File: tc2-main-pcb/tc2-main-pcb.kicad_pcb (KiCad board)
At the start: 4 copper layers, 73 x 75.5 mm, 191 parts, among them J1 Screw_Terminal_01x01, J10 Conn_02x06_Odd_Even, J11 Conn_01x08, J12 USB_B_Micro, J2 Screw_Terminal_01x01, J3 Conn_01x03, J4 Raspberry_Pi_2_3, J5 Screw_Terminal_01x01, J6 Screw_Terminal_01x01, J7 Screw_Terminal_01x01, J8 Screw_Terminal_01x01, J9 Conn_02x03_Odd_Even, Q1 Q_PMOS_GSD, SW1 SW_Push, U1 ATtiny1616-M, U10 TD6810, U11 TD6810, U12 SIM7600G-H-M.2, U13 AHT20_C2757850, U14 MAX98357AEWL+T, U15 74HC4052, U16 M24C02-WMN, U18 TCA4311ADGKR, U2 W25Q128JVS, U3 RP2040, U4 MT29F2G01ABAGDWB-IT, U5 TPS6302x, U6 PCF8563T, U7 ME6216A28XG, U8 Flir_LEPTON, U9 3N25000G33YC, Y1 Crystal_GND24, Y2 Crystal

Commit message: panelize WIP
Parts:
- added REF**: Tab, kikit:Tab, F.Cu at (12.2, -28.0)
- added REF**: Tab, kikit:Tab, F.Cu at (-54.8, -22.0)
- added REF**: Tab, kikit:Tab, F.Cu at (3.80, -37.0)
- added REF**: Tab, kikit:Tab, F.Cu at (-61.8, 20.0)
- added REF**: Tab, kikit:Tab, F.Cu at (-5.79, 34.0)
- added REF**: Tab, kikit:Tab, F.Cu at (-36.2, -37.0)
- added REF**: Tab, kikit:Tab, F.Cu at (12.8, 22.0)
- added REF**: Tab, kikit:Tab, F.Cu at (-16.2, -37.0)
- added REF**: Tab, kikit:Tab, F.Cu at (-51.8, 27.0)
- BT1, C1, C16, C17, C18, C19, C2, C20, C21, C22, C23, C24, C32, C33, C34, C35, C36, C39, C40, C51, C56, C57, C58, C59, C61, C62, C63, D2, D3, J1, J10, J11, J12, J2, J3, J4, J5, J6, J8, R1, R10, R11, R13, R14, R15, R17, R2, R25, R26, R27, R32, R35, R36, R37, R39, R46, R49, R50, R51, R6, R7, R8, TP17, U1, U12, U13, U2, U4, U6, U7, U9, Y2: moved to F.Cu
- C10, C11, C12, C13, C14, C15, C25, C26, C27, C28, C29, C3, C30, C31, C37, C38, C4, C41, C42, C43, C44, C45, C46, C47, C48, C49, C5, C50, C52, C53, C54, C55, C6, C60, C64, C65, C66, C7, C8, C9, FB1, H1, H2, H3, H4, H5, H6, J7, J9, L1, L2, L3, LED1, Q1, R12, R16, R18, R19, R20, R21, R22, R23, R24, R28, R29, R3, R30, R31, R33, R34, R38, R4, R40, R41, R42, R43, R44, R45, R47, R48, R5, R52, R53, R9, SW1, TP1, TP10, TP11, TP12, TP13, TP14, TP15, TP16, TP18, TP19, TP2, TP20, TP21, TP22, TP26, TP27, TP3, TP4, TP40, TP41, TP5, TP6, TP7, TP8, U10, U11, U14, U15, U16, U18, U3, U5, U8, Y1: moved to B.Cu
- moved H2 113.6 mm to (-56.8, 18.0), turned to 180 degrees
- moved J11 103.4 mm to (-51.7, -11.0), turned to 0 degrees
- moved J1 98.0 mm to (-49.0, -29.0), turned to 0 degrees
- moved J8 98.0 mm to (-49.0, 21.0), turned to 0 degrees
- moved C33 89.8 mm to (-44.9, 10.2)
- moved C36 87.4 mm to (-43.7, 10.8)
- moved TP18 86.7 mm to (-43.3, -16.5), turned to 180 degrees
- moved TP14 86.6 mm to (-43.3, -18.3), turned to 180 degrees
- moved C34 85.0 mm to (-42.5, 10.2)
- moved C25 84.4 mm to (-42.2, 3.58)
- moved TP19 84.2 mm to (-42.1, -1.90), turned to 180 degrees
- moved H1 83.6 mm to (-41.8, -29.0), turned to 180 degrees
- moved FB1 83.6 mm to (-41.8, 15.3)
- moved C40 82.7 mm to (-41.3, 10.8)
- moved TP20 82.4 mm to (-41.2, -8.00), turned to 180 degrees
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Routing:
- added copper zone on B.Cu, net +3V3_rp2040
- added copper zone on B.Cu, net /Lepton/SW_1V2
- added copper zone on B.Cu, net /Lepton/SW_3V0
- added copper zone on B.Cu, net /modem/3V3_L1
- added copper zone on B.Cu, net /modem/3V3_L2
- added copper zone on B.Cu, net /modem/MODEM_3V8
- removed copper zone on F.Cu, net +3V3_rp2040
- removed copper zone on F.Cu, net /Lepton/SW_1V2
- removed copper zone on F.Cu, net /Lepton/SW_3V0
- removed copper zone on F.Cu, net /modem/3V3_L1
- removed copper zone on F.Cu, net /modem/3V3_L2
- removed copper zone on F.Cu, net /modem/MODEM_3V8
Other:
- outline, holes or cut-outs redrawn

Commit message: Adding panel
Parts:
- removed the REF** at (12.2, -28.0)
- removed the REF** at (-54.8, -22.0)
- removed the REF** at (3.80, -37.0)
- removed the REF** at (-61.8, 20.0)
- removed the REF** at (-5.79, 34.0)
- removed the REF** at (-36.2, -37.0)
- removed the REF** at (12.8, 22.0)
- removed the REF** at (-16.2, -37.0)
- removed the REF** at (-51.8, 27.0)
- added REF**: Tab_8mm, kikit:Tab_8mm, F.Cu at (12.2, 22.0)
- added REF**: Tab_8mm, kikit:Tab_8mm, F.Cu at (-36.2, -36.4)
- added REF**: Tab_8mm, kikit:Tab_8mm, F.Cu at (3.80, -36.3)
- added REF**: Tab_8mm, kikit:Tab_8mm, F.Cu at (12.6, -28.0)
- added REF**: Tab_8mm, kikit:Tab_8mm, F.Cu at (-62.1, 20.0)
- added REF**: Tab_8mm, kikit:Tab_8mm, F.Cu at (-5.80, 34.3)
- added REF**: Tab_8mm, kikit:Tab_8mm, F.Cu at (-55.1, -22.0)
- added REF**: Tab_8mm, kikit:Tab_8mm, F.Cu at (-51.8, 27.3)
- added REF**: Tab_8mm, kikit:Tab_8mm, F.Cu at (-16.2, -36.4)

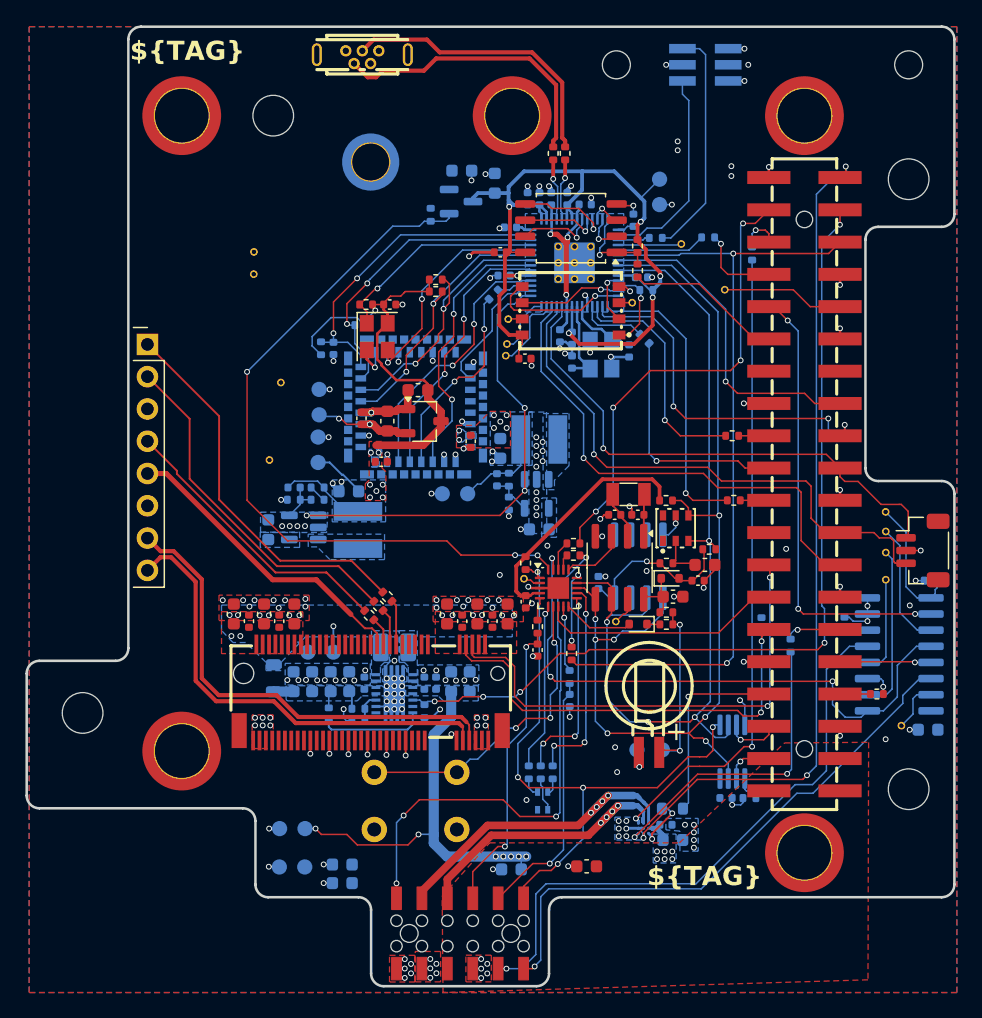
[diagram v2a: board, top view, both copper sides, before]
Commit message: Update to use touch sensor
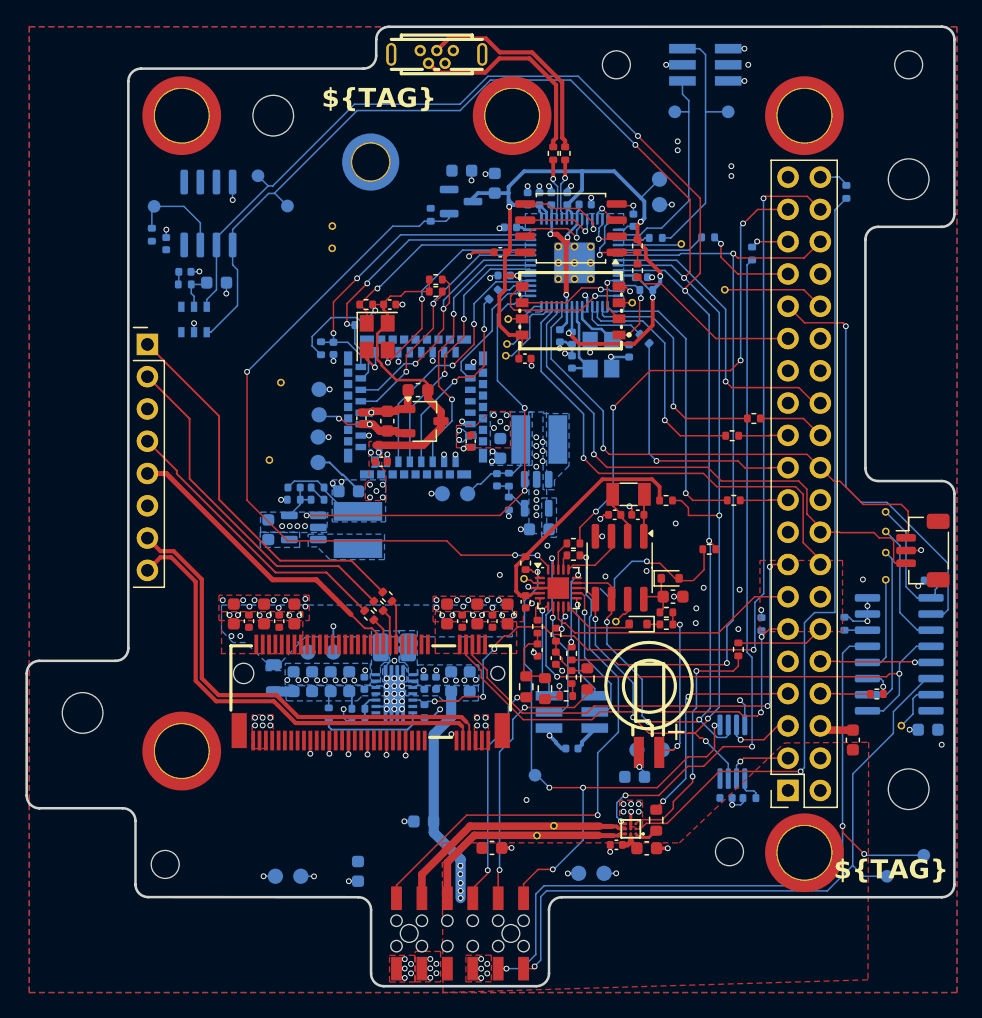
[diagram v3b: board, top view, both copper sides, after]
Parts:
- removed LED1: NH-B1515RGBA-HF, cacophony-library:LED-ARRAY-SMD_4P-L1.6-W1.5-TL_NH-B1515RGBA
- removed R3, R4, R5: 180R, Resistor_SMD:R_0402_1005Metric
- removed the REF** at (12.2, 22.0)
- removed the REF** at (-36.2, -36.4)
- removed the REF** at (3.80, -36.3)
- removed the REF** at (12.6, -28.0)
- removed the REF** at (-62.1, 20.0)
- removed the REF** at (-5.80, 34.3)
- removed the REF** at (-55.1, -22.0)
- removed the REF** at (-51.8, 27.3)
- removed the REF** at (-16.2, -36.4)
- removed SW1: SW_Push, Button_Switch_THT:SW_PUSH_6mm
- added C131: 22uF, Capacitor_SMD:C_0603_1608Metric, F.Cu at (3.81, 20.1)
- added C168: 220nF, Capacitor_SMD:C_0402_1005Metric, B.Cu at (-18.3, 20.8)
- added H107: MountingHole, cacophony-library:MountingHole_2.2mm_M2, F.Cu at (-50.3, 29.9)
- added H108: MountingHole, cacophony-library:MountingHole_2.2mm_M2, F.Cu at (-5.90, 28.9)
- added J113: Conn_02x03_Odd_Even, cacophony-library:mic-pcb, B.Cu at (-18.3, 17.9)
- added R115: 100k, Resistor_SMD:R_0402_1005Metric, B.Cu at (-51.4, -19.6)
- added R146: 1M, Resistor_SMD:R_0603_1608Metric, F.Cu at (-21.9, 15.9)
- added R148: 680k, Resistor_SMD:R_0603_1608Metric, F.Cu at (-20.4, 16.1)
- added R150: 1M, Resistor_SMD:R_0603_1608Metric, F.Cu at (-17.1, 15.3)
- added R152: 100k, Resistor_SMD:R_0402_1005Metric, F.Cu at (-18.3, 15.2)
- added R153: 68k, Resistor_SMD:R_0402_1005Metric, F.Cu at (-18.8, 16.7)
- added REF**: Tab8mm, cacophony-library:Tab8mm, F.Cu at (-55.1, -22.0)
- added REF**: Tab8mm, cacophony-library:Tab8mm, F.Cu at (-43.8, 35.3)
- added REF**: Tab8mm, cacophony-library:Tab8mm, F.Cu at (-5.80, 34.3)
- added REF**: Tab8mm, cacophony-library:Tab8mm, F.Cu at (-62.1, 20.0)
- added REF**: Tab8mm, cacophony-library:Tab8mm, F.Cu at (3.80, -36.3)
- added REF**: Tab8mm, cacophony-library:Tab8mm, F.Cu at (12.6, -28.0)
- added REF**: Tab8mm, cacophony-library:Tab8mm, F.Cu at (-16.2, -36.4)
- added REF**: Tab8mm, cacophony-library:Tab8mm, F.Cu at (-41.2, -36.4)
- added REF**: Tab8mm, cacophony-library:Tab8mm, F.Cu at (12.2, 22.0)
- added TP101: TestPoint, TestPoint:TestPoint_Pad_D1.0mm, B.Cu at (-6.00, -29.3)
- added TP102: TestPoint, TestPoint:TestPoint_Pad_D1.0mm, B.Cu at (-10.2, -29.3)
- added TP108: TestPoint, TestPoint:TestPoint_Pad_D1.0mm, B.Cu at (-40.7, -21.9)
- added TP110: TestPoint, TestPoint:TestPoint_Pad_D1.0mm, B.Cu at (-43.0, -24.3)
- added TP117: TestPoint, TestPoint:TestPoint_Pad_D1.0mm, B.Cu at (-51.2, -21.9)
- added TP120: TestPoint, cacophony-library:TP, F.Cu at (-21.1, 27.6)
- added TP121: TestPoint, TestPoint:TestPoint_Pad_D1.0mm, B.Cu at (-21.2, 22.9)
- added TP122: TestPoint, cacophony-library:TP, F.Cu at (-19.7, 26.9)
- added TP126: TestPoint, TestPoint:TestPoint_Pad_D1.0mm, B.Cu at (6.50, 30.9)
- added TP128: TestPoint, TestPoint:TestPoint_Pad_D1.0mm, B.Cu at (9.39, 29.2)
- C118: renamed from C17; moved to B.Cu
- C119: renamed from C39; moved to B.Cu
- C128: renamed from C28; moved to F.Cu
- C129: renamed from C29; moved to F.Cu
- C167: renamed from C44; moved to F.Cu
- J110: renamed from J4; footprint cacophony-library:HDR-SMD_40P-P2.54-V-F-R2-C20-LS8.2-EH -> cacophony-library:rpi-throughhole-socket
- R112: renamed from R39; moved to B.Cu
- R116: renamed from R12; moved to F.Cu
- R119: renamed from R34; moved to F.Cu
- R122: renamed from R31; moved to F.Cu
- R151: renamed from R40; moved to F.Cu
- U104: renamed from U13; moved to B.Cu
- U107: renamed from U14; moved to F.Cu
- moved C118 47.1 mm to (-48.8, -16.7)
- moved C119 44.4 mm to (-46.3, -15.9)
- moved R112 43.8 mm to (-48.8, -15.7)
- moved U106 43.8 mm to (-46.9, -21.3)
- moved C121 43.2 mm to (-50.2, -18.9)
- moved U104 41.3 mm to (-48.0, -13.0), turned to 90 degrees
- moved C124 24.5 mm to (-13.4, 23.0), turned to 0 degrees
- moved J110 24.1 mm to (-1.29, 24.1)
- moved TP119 23.8 mm to (-16.8, 30.6)
- moved C127 7.86 mm to (-30.0, 26.5)
- moved C126 7.59 mm to (-24.6, 28.6), turned to 0 degrees
- moved R122 6.78 mm to (-3.98, -5.17)
- moved TP104 6.50 mm to (-37.1, -20.3)
- moved TP105 6.50 mm to (-37.2, -18.6)
- moved J102 5.86 mm to (-28.9, -33.6)
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- renumbered BT1 to BT101, C5 to C101, C6 to C102, C8 to C103, C10 to C104, C11 to C105, C12 to C106, C13 to C107, C14 to C108, C15 to C109, C38 to C110, C43 to C111, C7 to C112, C9 to C113, C2 to C114, C3 to C115, C4 to C116, C16 to C117, C18 to C120, C48 to C121, C63 to C122, C61 to C123, C65 to C124, C66 to C125, C62 to C126, C64 to C127, C50 to C130, C37 to C132, C25 to C133, C41 to C134, C30 to C135, C26 to C136, C21 to C137, C23 to C138, C42 to C139, C31 to C140, C24 to C141, C19 to C142, C20 to C143, C22 to C144, C27 to C145, C54 to C146, C55 to C147, C47 to C148, C46 to C149, C45 to C150, C60 to C151, C49 to C152, C52 to C153, C53 to C154, C57 to C155, C58 to C156, C59 to C157, C51 to C158, C32 to C159, C33 to C160, C34 to C161, C35 to C162, C36 to C163, C40 to C164, C56 to C165, C1 to C166, D3 to D101, D2 to D102, FB1 to FB101, H5 to H101, H6 to H102, H1 to H103, H3 to H104, H4 to H105, H2 to H106, J9 to J101, J12 to J102, J3 to J103, J10 to J104, J2 to J105, J8 to J106, J1 to J107, J5 to J108, J6 to J109, J11 to J111, J7 to J112, L1 to L101, L2 to L102, L3 to L103, Q1 to Q101, R38 to R101, R50 to R102, R51 to R103, R28 to R104, R10 to R105, R53 to R106, R11 to R107, R2 to R108, R1 to R109, R48 to R110, R9 to R111, R7 to R113, R8 to R114, R52 to R117, R37 to R118, R29 to R120, R30 to R121, R14 to R123, R32 to R124, R41 to R125, R47 to R126, R33 to R127, R20 to R128, R21 to R129, R22 to R130, R23 to R131, R17 to R132, R18 to R133, R19 to R134, R16 to R135, R13 to R136, R36 to R137, R42 to R138, R43 to R139, R45 to R140, R44 to R141, R24 to R142, R25 to R143, R26 to R144, R27 to R145, R49 to R147, R6 to R149, R15 to R154, R46 to R155, R35 to R156, TP3 to TP103, TP14 to TP104, TP18 to TP105, TP19 to TP106, TP20 to TP107, TP12 to TP109, TP26 to TP111, TP27 to TP112, TP41 to TP113, TP40 to TP114, TP13 to TP115, TP17 to TP116, TP6 to TP118, TP10 to TP119, TP22 to TP123, TP16 to TP124, TP15 to TP125, TP21 to TP127, TP11 to TP129, TP7 to TP130, TP4 to TP131, TP8 to TP132, TP5 to TP133, TP1 to TP134, TP2 to TP135, U2 to U101, U3 to U102, U4 to U103, U6 to U105, U16 to U106, U18 to U108, U15 to U109, U10 to U110, U11 to U111, U7 to U112, U9 to U113, U8 to U114, U5 to U115, U12 to U116, U1 to U117, Y1 to Y101, Y2 to Y102
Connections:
- net BATT_SENSE_HIGH_VOLTAGE_PHY renamed BATT_SENSE_HV_PHY
- net BATT_SENSE_LOW_VOLTAGE_PHY renamed BATT_SENSE_LV_PHY
- C165 pad 2: BATT_SENSE_LV -> /ATtiny1616/BATT_SENSE_LV
- C167 pad 2: BATT_SENSE_HV -> /ATtiny1616/BATT_SENSE_HV
- J104 pad 3: BATT_SENSE_HV -> BATTERY_HV
- J104 pad 5: BATT_SENSE_LV -> BATTERY_LV
- J104 pad 7: SPEAKER_- -> SPEAKER_+
- J104 pad 9: SPEAKER_+ -> SPEAKER_-
- R147 pad 2: BATT_SENSE_LV -> /ATtiny1616/BATT_SENSE_LV
- R151 pad 2: BATT_SENSE_HV -> /ATtiny1616/BATT_SENSE_HV
- U106 pad 7: unconnected-(U16-~{WC}-Pad7) -> /EEPROM_~{WC}
- U117 pad 11: /ATtiny1616/~{LED_B_PHY} -> ~{LED_B}
- U117 pad 12: /ATtiny1616/~{LED_G_PHY} -> ~{LED_G}
- U117 pad 6: /ATtiny1616/~{LED_R_PHY} -> ~{LED_R}
- U117 pad 7: /ATtiny1616/ATtiny_SW -> ATtiny_SW
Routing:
- net SCL: track 71.8 -> 125.8 mm, vias 4 -> 6
- net SDA: track 79.9 -> 132.9 mm
- net /ATtiny1616/ATtiny_SW: track 24.7 -> 0.00 mm, vias 3 -> 0
- net BATT_SENSE_LV: track 23.7 -> 0.00 mm, vias 2 -> 0
- net BATTERY_HV: track 0.00 -> 21.6 mm, vias 0 -> 2
- net BATT_SENSE_HV: track 20.0 -> 0.00 mm, vias 1 -> 0
- net BATTERY_LV: track 0.00 -> 17.2 mm, vias 0 -> 2
- net /ATtiny1616/~{LED_G_PHY}: track 16.4 -> 0.00 mm, vias 3 -> 0
- net /ATtiny1616/~{LED_B_PHY}: track 15.6 -> 0.00 mm, vias 3 -> 0
- net +5V: track 34.4 -> 20.8 mm, vias 13 -> 6
- net /ATtiny1616/~{LED_R_PHY}: track 13.2 -> 0.00 mm, vias 1 -> 0
- net OUT_TX: track 47.0 -> 59.7 mm, vias 1 -> 3
- net GND: track 105.8 -> 96.1 mm, vias 183 -> 178
- net ~{LED_G}: track 1.32 -> 10.9 mm, vias 0 -> 1
- net ATtiny_SW: track 0.00 -> 9.01 mm, vias 0 -> 1
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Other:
- outline, holes or cut-outs redrawn

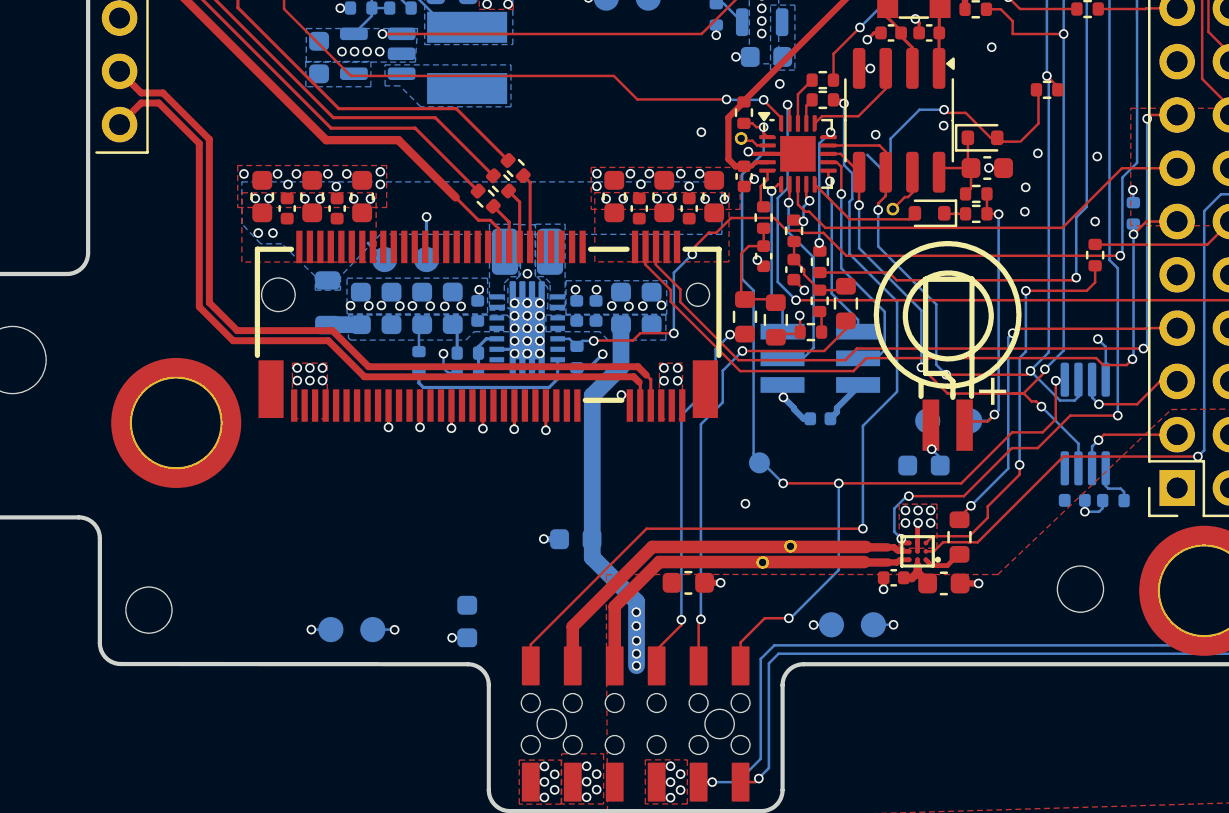
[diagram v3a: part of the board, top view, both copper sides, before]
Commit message: Change to through hole connector and add simcard PCB to pannel
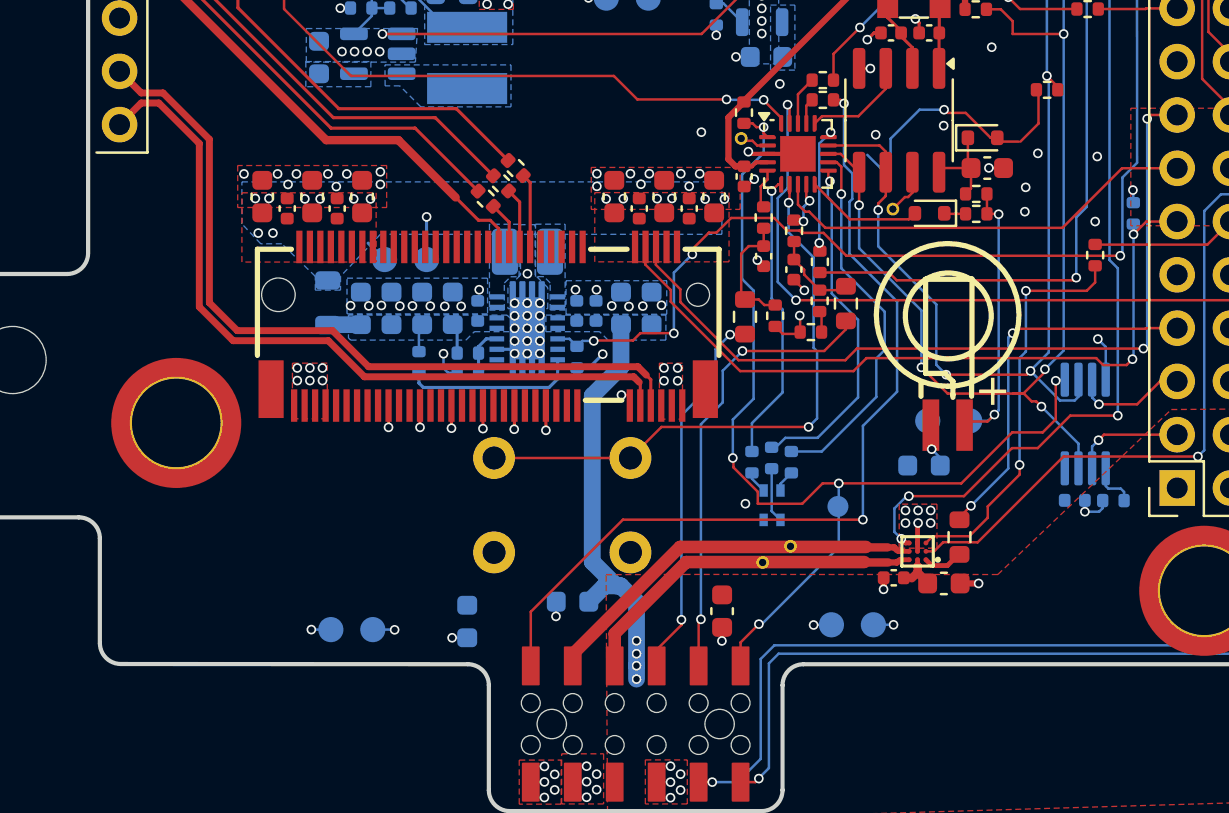
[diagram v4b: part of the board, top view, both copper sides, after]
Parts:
- removed C168: 220nF, Capacitor_SMD:C_0402_1005Metric
- removed H107, H108: MountingHole, cacophony-library:MountingHole_2.2mm_M2
- removed J113: Conn_02x03_Odd_Even, cacophony-library:mic-pcb
- removed R148: 680k, Resistor_SMD:R_0603_1608Metric
- added LED101: NH-B1515RGBA-HF, cacophony-library:LED-ARRAY-SMD_4P-L1.6-W1.5-TL_NH-B1515RGBA, B.Cu at (-20.6, 24.9)
- added R157: 180R, Resistor_SMD:R_0402_1005Metric, B.Cu at (-21.6, 22.9)
- added R158: 180R, Resistor_SMD:R_0402_1005Metric, B.Cu at (-19.7, 22.9)
- added R159: 180R, Resistor_SMD:R_0402_1005Metric, B.Cu at (-20.6, 22.7)
- added R160: 470k, Resistor_SMD:R_0402_1005Metric, F.Cu at (-20.4, 15.9)
- added SW101: SW_Push, Button_Switch_THT:SW_PUSH_6mm, B.Cu at (-27.4, 22.7)
- C165, C167: value 12pF -> 22pF
- moved REF** 8.00 mm to (-4.20, -36.3)
- moved REF** 8.00 mm to (-24.2, -36.4)
- moved TP121 4.28 mm to (-17.5, 25.0)
- moved REF** 4.00 mm to (-45.2, -36.4)
- moved C127 2.98 mm to (-30.1, 29.5)
- moved C126 2.10 mm to (-23.0, 30.0), turned to -90 degrees
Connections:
- U117 pad 11: ~{LED_B} -> Net-(U117-PB3)
- U117 pad 12: ~{LED_G} -> Net-(U117-PB2)
- U117 pad 6: ~{LED_R} -> Net-(U117-PA5)
- U117 pad 7: ATtiny_SW -> Net-(U117-PA6)
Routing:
- net Net-(U117-PA6): track 0.00 -> 27.9 mm, vias 0 -> 2
- net Net-(U117-PB2): track 0.00 -> 17.8 mm, vias 0 -> 1
- net Net-(U117-PB3): track 0.00 -> 16.6 mm, vias 0 -> 1
- net Net-(U117-PA5): track 0.00 -> 13.8 mm, vias 0 -> 1
- net ~{LED_G}: track 10.9 -> 1.06 mm, vias 1 -> 0
- net ATtiny_SW: track 9.01 -> 0.00 mm, vias 1 -> 0
- net ~{LED_R}: track 7.51 -> 1.07 mm, vias 1 -> 0
- net ~{LED_B}: track 8.34 -> 2.41 mm, vias 1 -> 0
- net +5V: track 20.8 -> 23.4 mm, vias 6 -> 5
- net GND: track 96.1 -> 93.9 mm, vias 178 -> 177
- net 5V_EN: track 47.7 -> 50.0 mm
- net +3V3: track 36.9 -> 34.8 mm
- net SPEAKER_-: track 19.6 -> 18.2 mm
- net SPEAKER_+: track 17.8 -> 17.0 mm
- net EN_PERIPH_POWER: track 41.8 -> 42.5 mm
